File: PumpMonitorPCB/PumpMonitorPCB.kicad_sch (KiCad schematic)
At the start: 4 parts

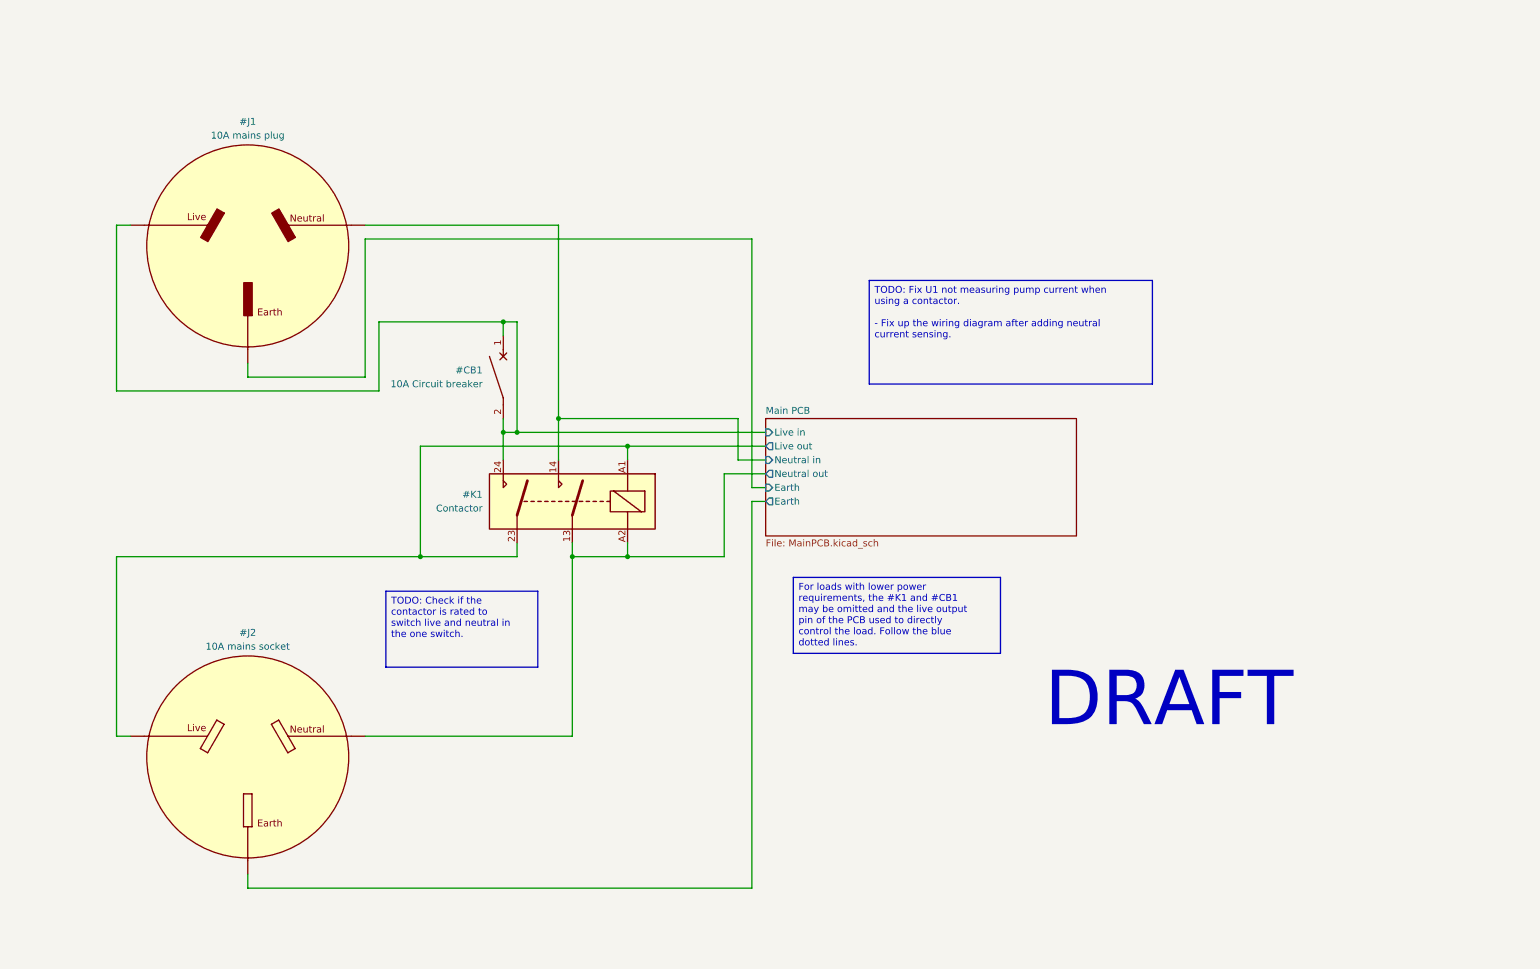
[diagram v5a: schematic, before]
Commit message: Made smaller mains connector symbols, added multiple options to wiring diagram,
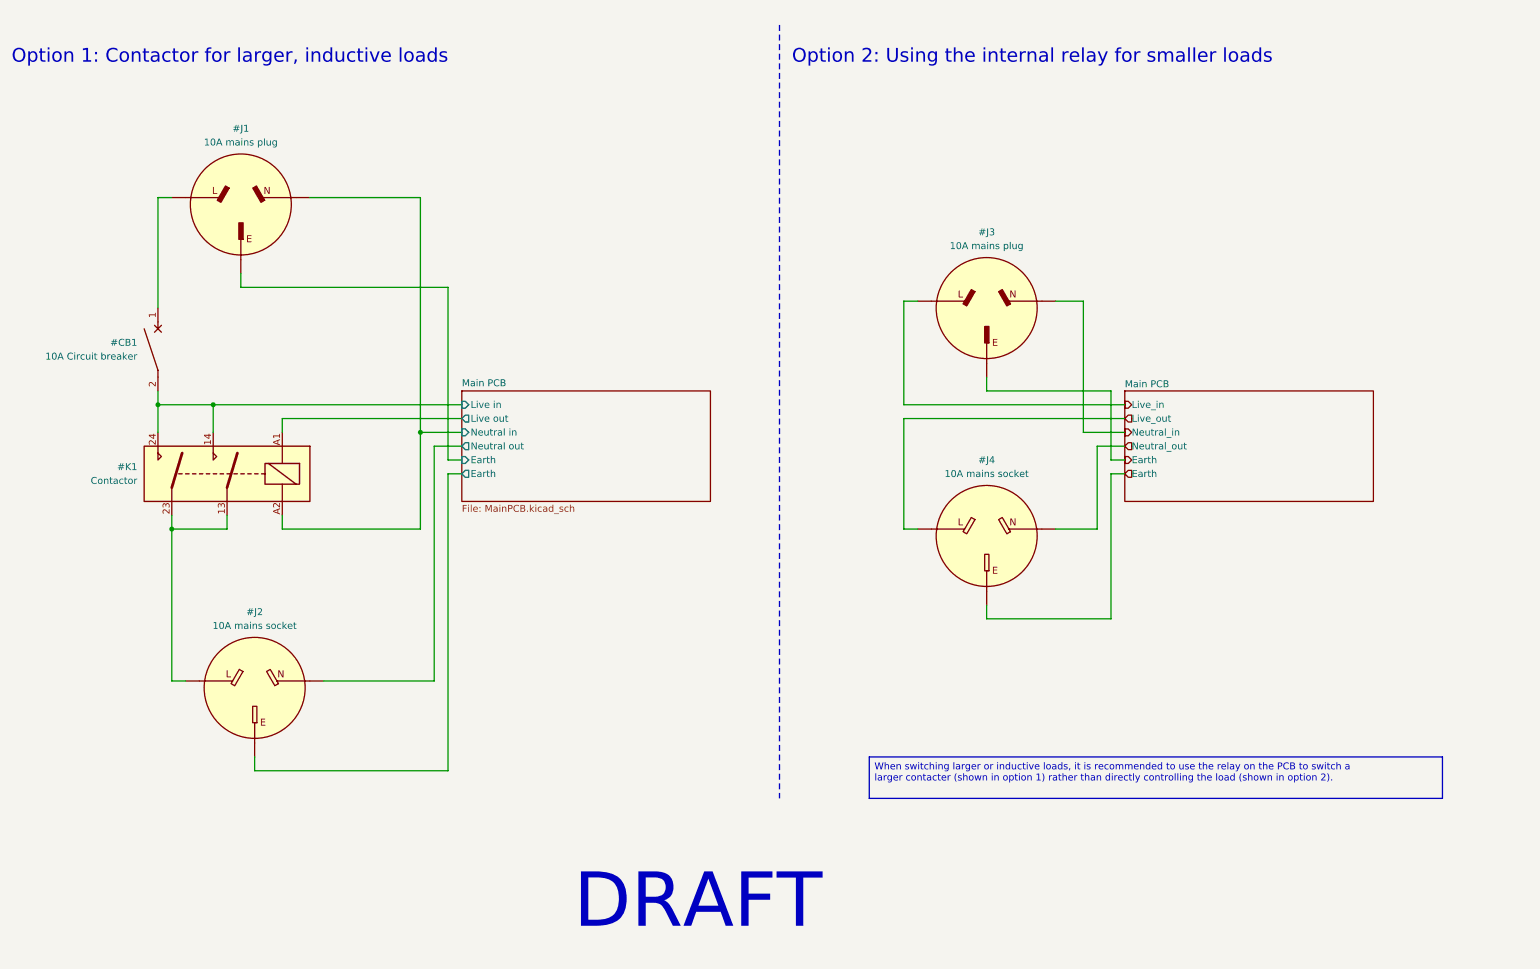
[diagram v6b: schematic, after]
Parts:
- removed #J1: 10A mains plug, symbol AustralianPowerpoints:3PinMainsPowerPlug
- removed #J2: 10A mains socket, symbol AustralianPowerpoints:3PinMainsPowerSocket
- added #J1, #J3: 10A mains plug, symbol AustralianPowerpoints:3PinMainsPowerPlug_Small
- added #J2, #J4: 10A mains socket, symbol AustralianPowerpoints:3PinMainsPowerSocket_Small
- added #MOD1: Main PCB, symbol PumpMonitorCustom:MainPCB
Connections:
- net Main PCB/Earth: now also #J2.3 (Earth)
- net Main PCB/Live in: now also #K1.14; no longer #CB1.1
- net Main PCB/Live out: no longer #K1.23
- net Main PCB/Neutral in: now also #K1.A2, #J1.2 (Neutral); no longer #K1.14
- net Main PCB/Neutral out: now also #J2.2 (Neutral); no longer #K1.13, #K1.A2
- new net: #CB1.1, #J1.1 (Live)
- new net: #J3.1 (Live), #MOD1.1 (Live_in)
- new net: #J4.1 (Live), #MOD1.2 (Live_out)
- new net: #J3.2 (Neutral), #MOD1.3 (Neutral_in)
- new net: #J4.2 (Neutral), #MOD1.4 (Neutral_out)
- new net: #J3.3 (Earth), #MOD1.5 (Earth)
- new net: #J4.3 (Earth), #MOD1.6 (Earth)
- new net: #J2.1 (Live), #K1.13, #K1.23
- new net Main PCB/Earth: #J1.3 (Earth)
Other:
- note added: "Option 1: Contactor for larger, inductive loads"
- note added: "Option 2: Using the internal relay for smaller loads"

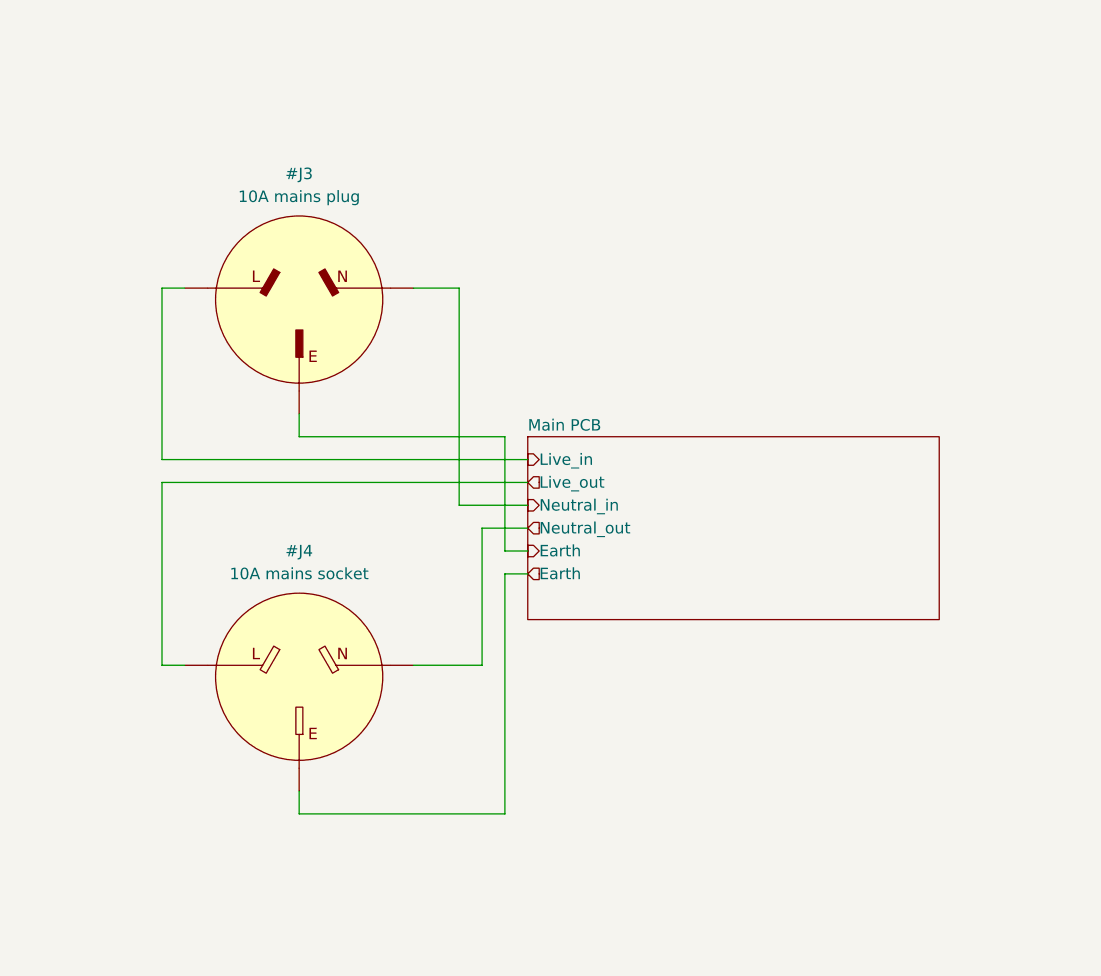
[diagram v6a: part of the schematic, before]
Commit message: Added terminals footprint and 3D model.
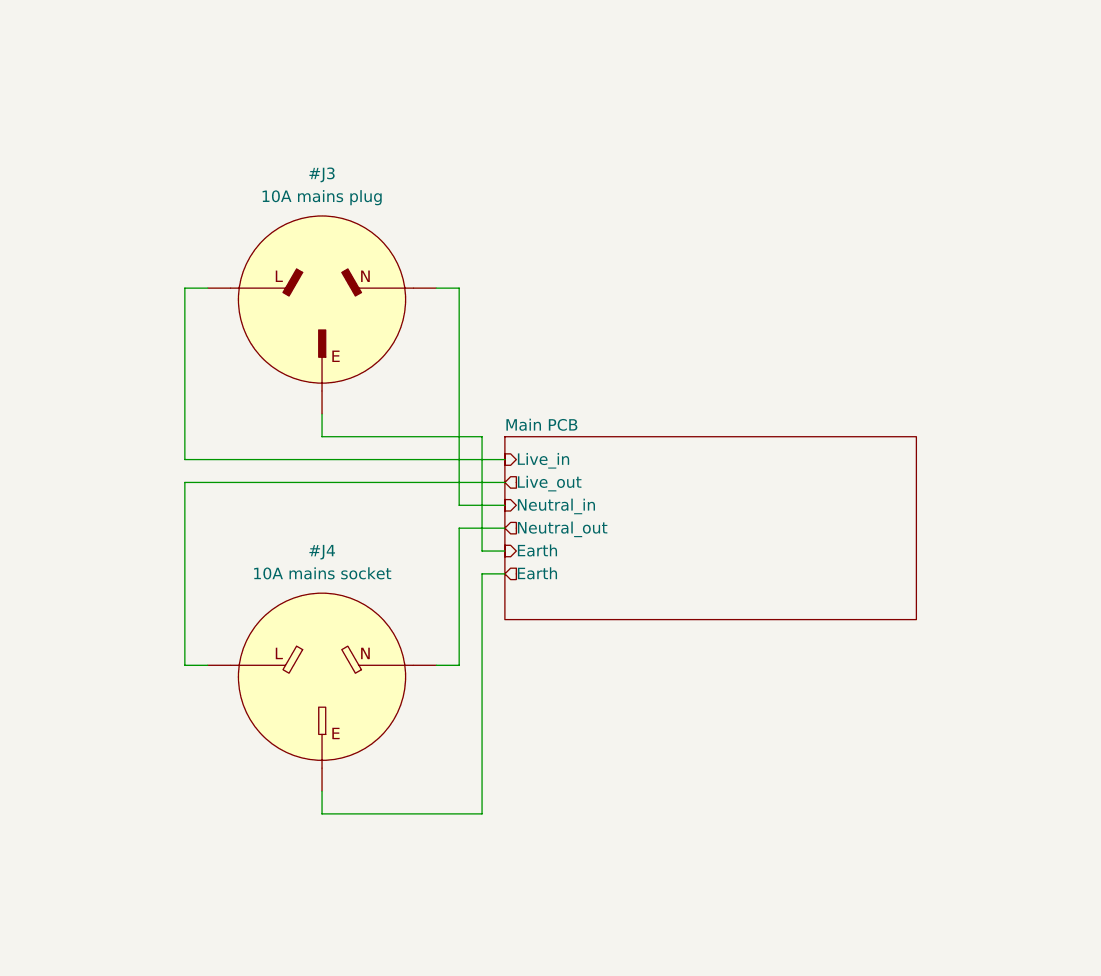
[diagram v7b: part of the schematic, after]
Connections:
- net Main PCB/Earth is gone; now on net Main PCB/Earth: #J2.3 (Earth)
- net Main PCB/Earth: no longer #J1.3 (Earth)
- new net Main PCB/Earth: #J1.3 (Earth)
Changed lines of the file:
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@@
 	(wire
 		(pts
-			(xy 222.25 104.14) (xy 224.79 104.14)
+			(xy 219.71 104.14) (xy 222.25 104.14)
 		)
 		(stroke
@@
 	(wire
 		(pts
-			(xy 222.25 130.81) (xy 222.25 104.14)
-		)
-		(stroke
-			(width 0)
-			(type default)
-		)
-	)
-	(wire
-		(pts
-			(xy 184.15 114.3) (xy 186.69 114.3)
+			(xy 219.71 130.81) (xy 219.71 104.14)
+		)
+		(stroke
+			(width 0)
+			(type default)
+		)
+	)
+	(wire
+		(pts
+			(xy 186.69 114.3) (xy 189.23 114.3)
 		)
 		(stroke
@@
 	(wire
 		(pts
-			(xy 219.71 99.06) (xy 219.71 114.3)
-		)
-		(stroke
-			(width 0)
-			(type default)
-		)
-	)
-	(wire
-		(pts
-			(xy 186.69 72.39) (xy 184.15 72.39)
+			(xy 217.17 99.06) (xy 217.17 114.3)
+		)
+		(stroke
+			(width 0)
+			(type default)
+		)
+	)
+	(wire
+		(pts
+			(xy 189.23 72.39) (xy 186.69 72.39)
 		)
 		(stroke
@@
 	(wire
 		(pts
-			(xy 212.09 72.39) (xy 217.17 72.39)
+			(xy 214.63 72.39) (xy 217.17 72.39)
 		)
 		(stroke
@@
 	(wire
 		(pts
-			(xy 222.25 101.6) (xy 222.25 88.9)
+			(xy 219.71 101.6) (xy 219.71 88.9)
 		)
 		(stroke
@@
 	(wire
 		(pts
-			(xy 219.71 114.3) (xy 212.09 114.3)
-		)
-		(stroke
-			(width 0)
-			(type default)
-		)
-	)
-	(wire
-		(pts
-			(xy 224.79 101.6) (xy 222.25 101.6)
+			(xy 217.17 114.3) (xy 214.63 114.3)
+		)
+		(stroke
+			(width 0)
+			(type default)
+		)
+	)
+	(wire
+		(pts
+			(xy 222.25 101.6) (xy 219.71 101.6)
 		)
 		(stroke
@@
 	(wire
 		(pts
-			(xy 222.25 88.9) (xy 199.39 88.9)
-		)
-		(stroke
-			(width 0)
-			(type default)
-		)
-	)
-	(wire
-		(pts
-			(xy 199.39 130.81) (xy 222.25 130.81)
-		)
-		(stroke
-			(width 0)
-			(type default)
-		)
-	)
-	(wire
-		(pts
-			(xy 199.39 128.27) (xy 199.39 130.81)
+			(xy 219.71 88.9) (xy 201.93 88.9)
+		)
+		(stroke
+			(width 0)
+			(type default)
+		)
+	)
+	(wire
+		(pts
+			(xy 201.93 130.81) (xy 219.71 130.81)
+		)
+		(stroke
+			(width 0)
+			(type default)
+		)
+	)
+	(wire
+		(pts
+			(xy 201.93 128.27) (xy 201.93 130.81)
 		)
 		(stroke
@@
 	(wire
 		(pts
-			(xy 199.39 88.9) (xy 199.39 86.36)
+			(xy 201.93 88.9) (xy 201.93 86.36)
 		)
 		(stroke
@@
 	(wire
 		(pts
-			(xy 184.15 93.98) (xy 184.15 114.3)
+			(xy 186.69 93.98) (xy 186.69 114.3)
 		)
 		(stroke
@@
 	(wire
 		(pts
-			(xy 184.15 72.39) (xy 184.15 91.44)
+			(xy 186.69 72.39) (xy 186.69 91.44)
 		)
 		(stroke
@@
 	(wire
 		(pts
-			(xy 184.15 91.44) (xy 224.79 91.44)
+			(xy 186.69 91.44) (xy 222.25 91.44)
 		)
 		(stroke
@@
 	(wire
 		(pts
-			(xy 224.79 99.06) (xy 219.71 99.06)
+			(xy 222.25 99.06) (xy 217.17 99.06)
 		)
 		(stroke
@@
 	(wire
 		(pts
-			(xy 184.15 93.98) (xy 224.79 93.98)
-		)
-		(stroke
-			(width 0)
-			(type default)
-		)
-	)
-	(wire
-		(pts
-			(xy 217.17 96.52) (xy 224.79 96.52)
+			(xy 186.69 93.98) (xy 222.25 93.98)
+		)
+		(stroke
+			(width 0)
+			(type default)
+		)
+	)
+	(wire
+		(pts
+			(xy 217.17 96.52) (xy 222.25 96.52)
 		)
 		(stroke
@@
 	(symbol
 		(lib_id "PumpMonitorCustom:MainPCB")
-		(at 247.65 86.36 0)
+		(at 245.11 86.36 0)
 		(unit 1)
 		(exclude_from_sim no)
@@
 		(fields_autoplaced yes)
 		(property "Reference" "#MOD1"
-			(at 247.65 86.36 0)
+			(at 245.11 86.36 0)
 			(effects
 				(font
@@
 		)
 		(property "Value" "Main PCB"
-			(at 224.79 87.63 0)
+			(at 222.25 87.63 0)
 			(do_not_autoplace yes)
 			(effects
@@
 		)
 		(property "Footprint" ""
-			(at 247.65 86.36 0)
+			(at 245.11 86.36 0)
 			(effects
 				(font
@@
 		)
 		(property "Datasheet" ""
-			(at 247.65 86.36 0)
+			(at 245.11 86.36 0)
 			(effects
 				(font
@@
 		)
 		(property "Description" "Symbol that represents the main PCB of the pump monitor (used to show alternate wiring)."
-			(at 247.65 86.36 0)
+			(at 245.11 86.36 0)
 			(effects
 				(font
@@
 	(symbol
 		(lib_id "AustralianPowerpoints:3PinMainsPowerPlug_Small")
-		(at 199.39 73.66 0)
+		(at 201.93 73.66 0)
 		(unit 1)
 		(exclude_from_sim no)
@@
 		(fields_autoplaced yes)
 		(property "Reference" "#J3"
-			(at 199.39 59.69 0)
+			(at 201.93 59.69 0)
 			(effects
 				(font
@@
 		)
 		(property "Value" "10A mains plug"
-			(at 199.39 62.23 0)
+			(at 201.93 62.23 0)
 			(effects
 				(font
@@
 		)
 		(property "Footprint" ""
-			(at 199.39 73.66 0)
+			(at 201.93 73.66 0)
 			(effects
 				(font
@@
 		)
 		(property "Datasheet" ""
-			(at 199.39 73.66 0)
+			(at 201.93 73.66 0)
 			(effects
 				(font
@@
 		)
 		(property "Description" ""
-			(at 199.39 73.66 0)
+			(at 201.93 73.66 0)
 			(effects
 				(font
@@
 	(symbol
 		(lib_id "AustralianPowerpoints:3PinMainsPowerSocket_Small")
-		(at 199.39 115.57 0)
+		(at 201.93 115.57 0)
 		(unit 1)
 		(exclude_from_sim no)
@@
 		(dnp no)
 		(property "Reference" "#J4"
-			(at 199.39 101.6 0)
+			(at 201.93 101.6 0)
 			(effects
 				(font
@@
 		)
 		(property "Value" "10A mains socket"
-			(at 199.39 104.14 0)
+			(at 201.93 104.14 0)
 			(effects
 				(font
@@
 		)
 		(property "Footprint" ""
-			(at 199.39 115.57 0)
+			(at 201.93 115.57 0)
 			(effects
 				(font
@@
 		)
 		(property "Datasheet" ""
-			(at 199.39 115.57 0)
+			(at 201.93 115.57 0)
 			(effects
 				(font
@@
 		)
 		(property "Description" ""
-			(at 199.39 115.57 0)
-			(effects
-				(font
+			(at 201.93 115.57 0)
+			(effects
+				(font
